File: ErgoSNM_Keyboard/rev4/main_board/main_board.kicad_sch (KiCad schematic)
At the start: 15 parts, among them J1 Conn_CoreBoard, J2 Conn_CoreBoard, J3 Conn_MouseSensor, J4 Conn_MouseSensor, J5 Conn_Batt, J6 Conn_Batt, SW1 RESET, SW2 RESET, SW3 SW_DPDT_x2, SW4 SW_DPDT_x2

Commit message: feat: add v4 mdbt50q board
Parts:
- removed TRRS1, TRRS2: PJ-393_TRRS_8P, ErgoSNM_Keyboard:PJ-393 8P TRRS, symbol ErgoSNM_Keyboard_Library:PJ-393_TRRS_8P
- added H1, H2, H3, H4, H5, H6: ~, MountingHole:MountingHole_2.2mm_M2_ISO7380, symbol Mechanical:MountingHole
- SB2: renamed from SB1; footprint Jumper:SolderJumper-2_P1.3mm_Open_TrianglePad1.0x1.5mm -> Jumper:SolderJumper-3_P2.0mm_Open_TrianglePad1.0x1.5mm_NumberLabels
- renumbered J3 to J1, J1 to J2, J4 to J3, J5 to J4, J6 to J5, J2 to J6, SB2 to SB1, SW3 to SW1, SW1 to SW2, SW2 to SW3
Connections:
- no-connect marks 10 -> 2

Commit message: feat: update main board layout
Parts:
- removed J4, J5: Conn_Batt, Connector_JST:JST_PH_S2B-PH-SM4-TB_1x02-1MP_P2.00mm_Horizontal, symbol Connector_Generic:Conn_01x02
- removed SB1: Batt Switch Bypass, Jumper:SolderJumper-2_P1.3mm_Open_TrianglePad1.0x1.5mm, symbol Jumper:SolderJumper_2_Open
- removed SB2: Charger Select, Jumper:SolderJumper-3_P2.0mm_Open_TrianglePad1.0x1.5mm_NumberLabels, symbol Jumper:SolderJumper_3_Open
- removed SW1, SW4: SW_DPDT_x2, ErgoSNM_Keyboard:MSKT-22D14-T, symbol Switch:SW_DPDT_x2
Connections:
- net IO_1 is gone; now on net VDD: J2.28 (Pin_28), J6.28 (Pin_28)
- net RX is gone; now on net COL_3: J2.8 (Pin_8), J6.8 (Pin_8)
- net TX is gone; now on net COL_4: J2.7 (Pin_7), J6.7 (Pin_7)
- net VBATT_{A} is gone; now on net GND: J2.1 (Pin_1), J6.1 (Pin_1)
- net COL_0: now also J2.11 (Pin_11), J6.11 (Pin_11); no longer J2.20 (Pin_20), J6.20 (Pin_20)
- net COL_1: now also J2.10 (Pin_10), J6.10 (Pin_10); no longer J2.21 (Pin_21), J6.21 (Pin_21)
- net COL_2: now also J2.9 (Pin_9), J6.9 (Pin_9); no longer J2.22 (Pin_22), J6.22 (Pin_22)
- net COL_3: no longer J2.23 (Pin_23), J6.23 (Pin_23)
- net COL_4: no longer J2.24 (Pin_24), J6.24 (Pin_24)
- net COL_5: now also J2.6 (Pin_6), J6.6 (Pin_6); no longer J2.25 (Pin_25), J6.25 (Pin_25)
- net GND: now also J2.25 (Pin_25), J2.5 (Pin_5), J6.25 (Pin_25), J6.5 (Pin_5); no longer J2.17 (Pin_17), J2.26 (Pin_26), J2.30 (Pin_30), J2.6 (Pin_6), J6.17 (Pin_17), J6.26 (Pin_26), J6.30 (Pin_30), J6.6 (Pin_6)
- net IO_0: now also J2.4 (Pin_4), J6.4 (Pin_4); no longer J2.27 (Pin_27), J6.27 (Pin_27)
- net MISO: now also J2.19 (Pin_19), J6.19 (Pin_19); no longer J2.12 (Pin_12), J6.12 (Pin_12)
- net MOSI: now also J2.20 (Pin_20), J6.20 (Pin_20); no longer J2.11 (Pin_11), J6.11 (Pin_11)
- net MOTION: now also J2.22 (Pin_22), J6.22 (Pin_22); no longer J2.9 (Pin_9), J6.9 (Pin_9)
- net RESET: now also J2.26 (Pin_26), J6.26 (Pin_26); no longer J2.5 (Pin_5), J6.5 (Pin_5)
- net ROW_0: now also J2.17 (Pin_17), J6.17 (Pin_17); no longer J2.14 (Pin_14), J6.14 (Pin_14)
- net ROW_1: now also J2.16 (Pin_16), J6.16 (Pin_16); no longer J2.15 (Pin_15), J6.15 (Pin_15)
- net ROW_2: now also J2.15 (Pin_15), J6.15 (Pin_15); no longer J2.16 (Pin_16), J6.16 (Pin_16)
- net ROW_3: now also J2.13 (Pin_13), J6.13 (Pin_13); no longer J2.18 (Pin_18), J6.18 (Pin_18)
- net ROW_4: now also J2.12 (Pin_12), J6.12 (Pin_12); no longer J2.19 (Pin_19), J6.19 (Pin_19)
- net SCLK: now also J2.21 (Pin_21), J6.21 (Pin_21); no longer J2.10 (Pin_10), J6.10 (Pin_10)
- net VDD: now also J2.27 (Pin_27), J6.27 (Pin_27); no longer J2.3 (Pin_3), J2.4 (Pin_4), J6.3 (Pin_3), J6.4 (Pin_4)
- net nCS: now also J2.18 (Pin_18), J6.18 (Pin_18); no longer J2.13 (Pin_13), J6.13 (Pin_13)
- net IO_2: no longer names the net of J2.29 (Pin_29)
- net IO_2: no longer J6.29 (Pin_29)
- net VBUS: no longer names the net of J2.2 (Pin_2)
- net VBUS: no longer J6.2 (Pin_2)
- no-connect marks 2 -> 14
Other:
- removed sheet Power
- note removed: "Ext. charger"
- note removed: "On board charger"
- moved on the sheet: J2, J6, R1, SW2, SW3

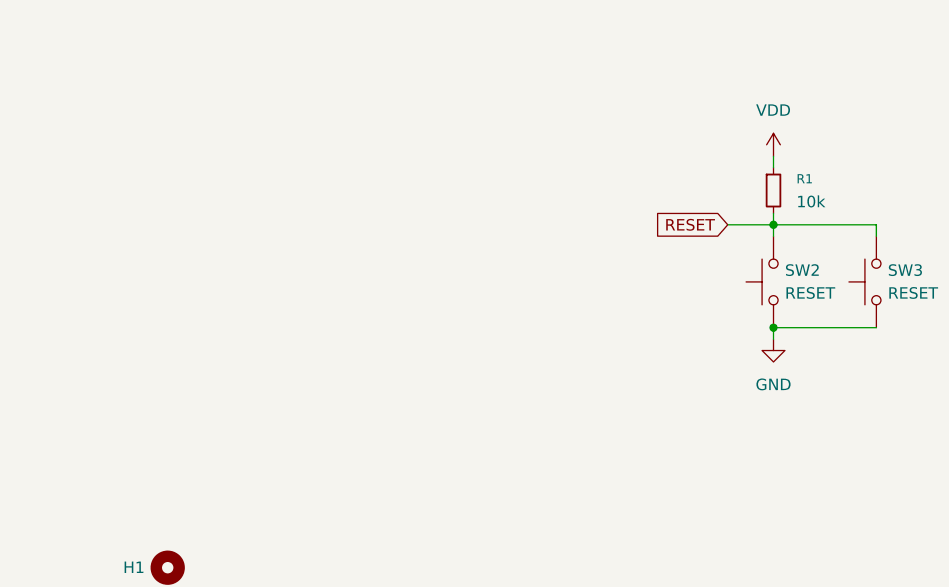
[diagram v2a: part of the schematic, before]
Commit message: feat: add 4x M2.5 mounting hole
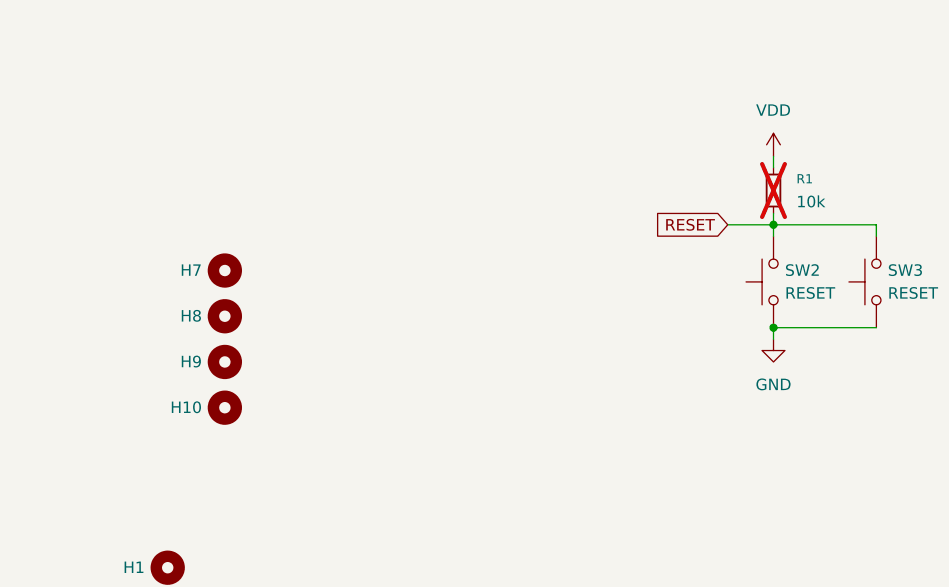
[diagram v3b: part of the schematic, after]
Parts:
- added H10, H7, H8, H9: ~, MountingHole:MountingHole_2.7mm_M2.5_ISO14580, symbol Mechanical:MountingHole
- R1: now not fitted

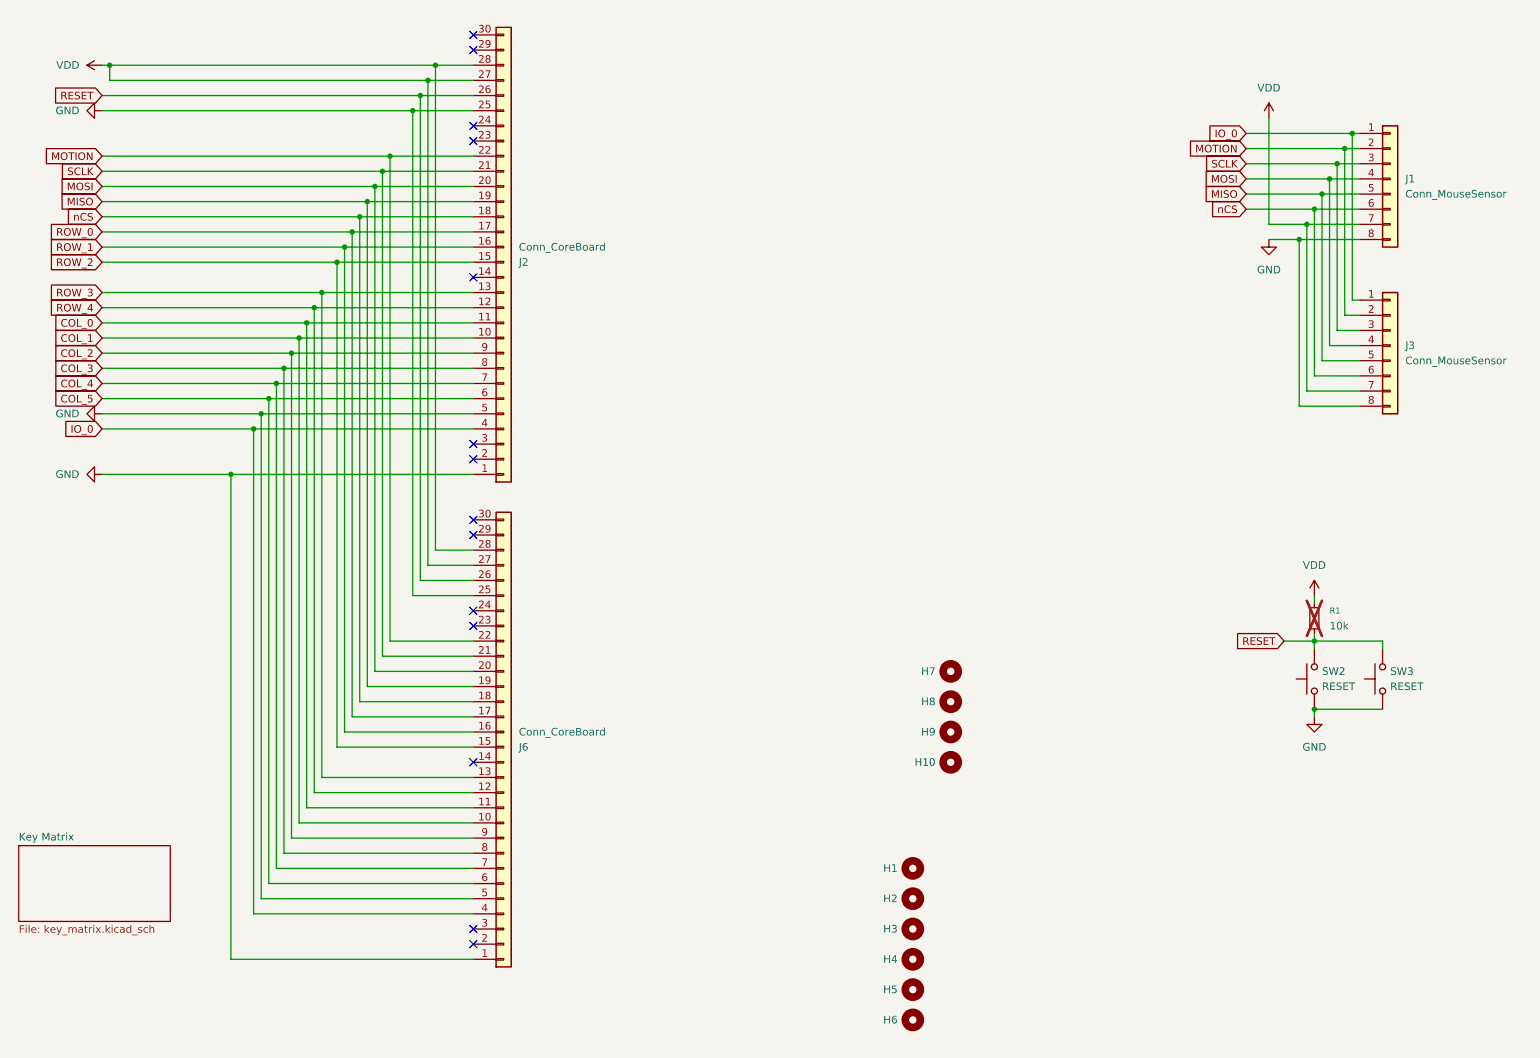
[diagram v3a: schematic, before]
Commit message: feat: update main board layout for 1.27mm pin header
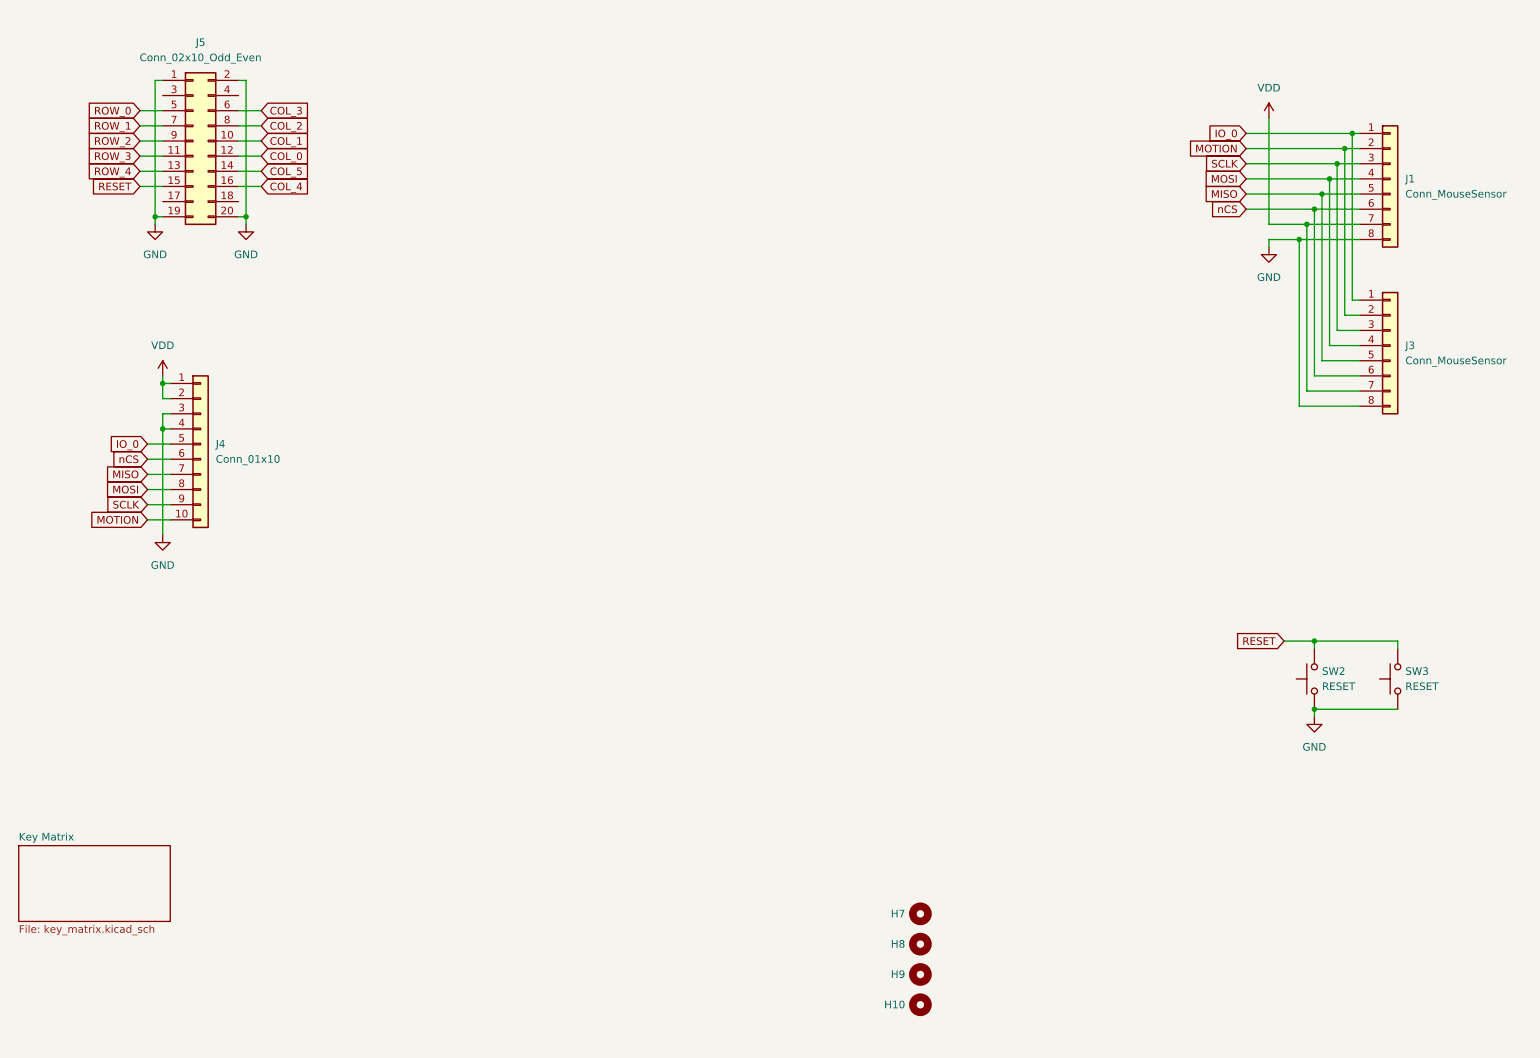
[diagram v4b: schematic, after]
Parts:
- removed H1, H2, H3, H4, H5, H6: ~, MountingHole:MountingHole_2.2mm_M2_ISO7380, symbol Mechanical:MountingHole
- removed J2, J6: Conn_CoreBoard, Connector_FFC-FPC:TE_3-1734839-0_1x30-1MP_P0.5mm_Horizontal, symbol Connector_Generic:Conn_01x30
- removed R1: 10k, Resistor_SMD:R_0603_1608Metric, symbol Device:R_Small
- added J4: Conn_01x10, Connector_PinSocket_1.27mm:PinSocket_1x10_P1.27mm_Vertical, symbol Connector_Generic:Conn_01x10
- added J5: Conn_02x10_Odd_Even, Connector_PinSocket_1.27mm:PinSocket_2x10_P1.27mm_Vertical, symbol Connector_Generic:Conn_02x10_Odd_Even
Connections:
- net COL_0: now also J5.12 (Pin_12)
- net COL_1: now also J5.10 (Pin_10)
- net COL_2: now also J5.8 (Pin_8)
- net COL_3: now also J5.6 (Pin_6)
- net COL_4: now also J5.16 (Pin_16)
- net COL_5: now also J5.14 (Pin_14)
- net GND: now also J4.3 (Pin_3), J4.4 (Pin_4), J5.1 (Pin_1), J5.19 (Pin_19), J5.2 (Pin_2), J5.20 (Pin_20)
- net IO_0: now also J4.5 (Pin_5)
- net MISO: now also J4.7 (Pin_7)
- net MOSI: now also J4.8 (Pin_8)
- net MOTION: now also J4.10 (Pin_10)
- net RESET: now also J5.15 (Pin_15)
- net ROW_0: now also J5.5 (Pin_5)
- net ROW_1: now also J5.7 (Pin_7)
- net ROW_2: now also J5.9 (Pin_9)
- net ROW_3: now also J5.11 (Pin_11)
- net ROW_4: now also J5.13 (Pin_13)
- net SCLK: now also J4.9 (Pin_9)
- net VDD: now also J4.1 (Pin_1), J4.2 (Pin_2)
- net nCS: now also J4.6 (Pin_6)
- no-connect marks 14 -> 0
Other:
- moved on the sheet: H10, H7, H8, H9, SW3

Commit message: feat: change pin header position
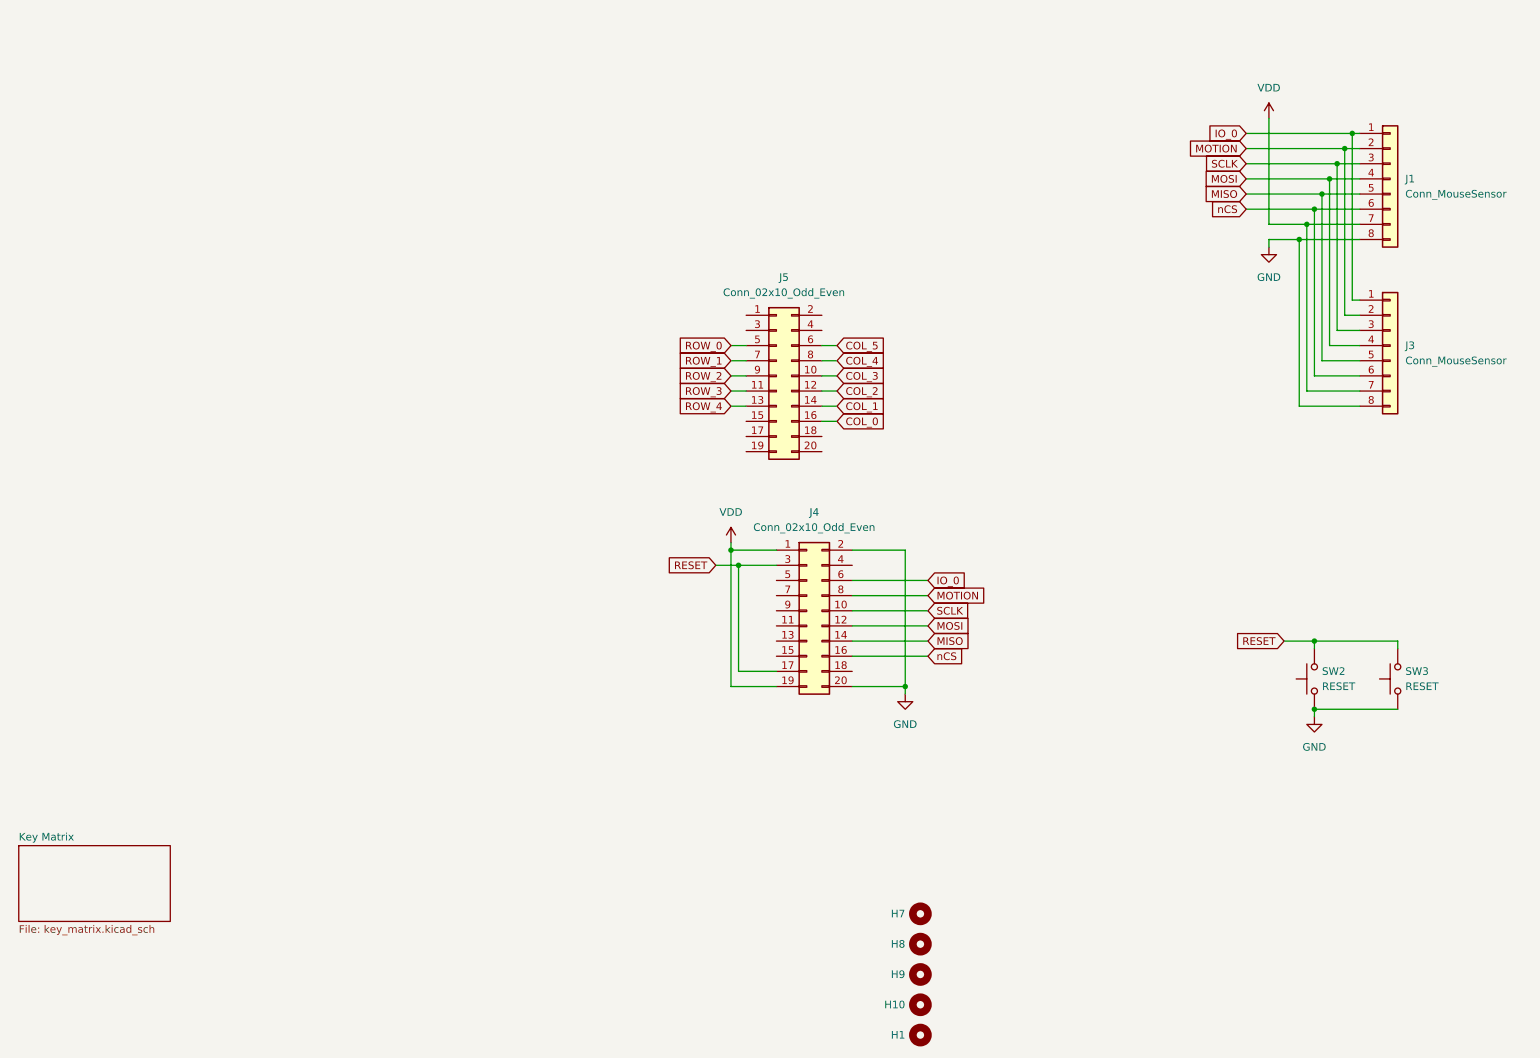
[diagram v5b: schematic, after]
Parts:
- removed J4: Conn_01x10, Connector_PinSocket_1.27mm:PinSocket_1x10_P1.27mm_Vertical, symbol Connector_Generic:Conn_01x10
- added H1: ~, MountingHole:MountingHole_2.7mm_M2.5_ISO14580, symbol Mechanical:MountingHole
- added J4: Conn_02x10_Odd_Even, Connector_PinSocket_1.27mm:PinSocket_2x10_P1.27mm_Vertical, symbol Connector_Generic:Conn_02x10_Odd_Even
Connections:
- net COL_0: now also J5.16 (Pin_16); no longer J5.12 (Pin_12)
- net COL_1: now also J5.14 (Pin_14); no longer J5.10 (Pin_10)
- net COL_2: now also J5.12 (Pin_12); no longer J5.8 (Pin_8)
- net COL_3: now also J5.10 (Pin_10); no longer J5.6 (Pin_6)
- net COL_4: now also J5.8 (Pin_8); no longer J5.16 (Pin_16)
- net COL_5: now also J5.6 (Pin_6); no longer J5.14 (Pin_14)
- net GND: now also J4.2 (Pin_2), J4.20 (Pin_20); no longer J5.1 (Pin_1), J5.19 (Pin_19), J5.2 (Pin_2), J5.20 (Pin_20)
- net IO_0: now also J4.6 (Pin_6)
- net MISO: now also J4.14 (Pin_14)
- net MOSI: now also J4.12 (Pin_12)
- net MOTION: now also J4.8 (Pin_8)
- net RESET: now also J4.17 (Pin_17), J4.3 (Pin_3); no longer J5.15 (Pin_15)
- net SCLK: now also J4.10 (Pin_10)
- net VDD: now also J4.1 (Pin_1), J4.19 (Pin_19)
- net nCS: now also J4.16 (Pin_16)
